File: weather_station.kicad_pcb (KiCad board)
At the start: 2 copper layers, 91.4 x 43.2 mm, 20 parts, among them J1 Barrel_Jack, U1 L7805, U2 LD1117S33TR, U6 NRF24L01_Breakout, U7 ATmega328-PU, Y1 16Mhz

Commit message: Poprawiona płytka (konektor NRF24 oraz otwory na śrubki)
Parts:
- U6: footprint RF_Module:nRF24L01_Breakout -> weather_station:NRF24-horizontal-pin-socket
- moved U6 11.4 mm to (146.6, 123.1), turned to 180 degrees
- moved C5 2.80 mm to (149.2, 107.7)
- renumbered RTC to U3, DHT22 to U4, LCD to U5
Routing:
- net /CSN: track 17.7 -> 6.76 mm
- net /MOSI: track 15.3 -> 5.70 mm
- net /SCK: track 10.3 -> 15.2 mm
- net /CE: track 13.4 -> 9.30 mm
- net +3V3: track 94.1 -> 97.3 mm
- net /MISO: track 10.3 -> 9.40 mm
- net GND: vias 28 -> 40

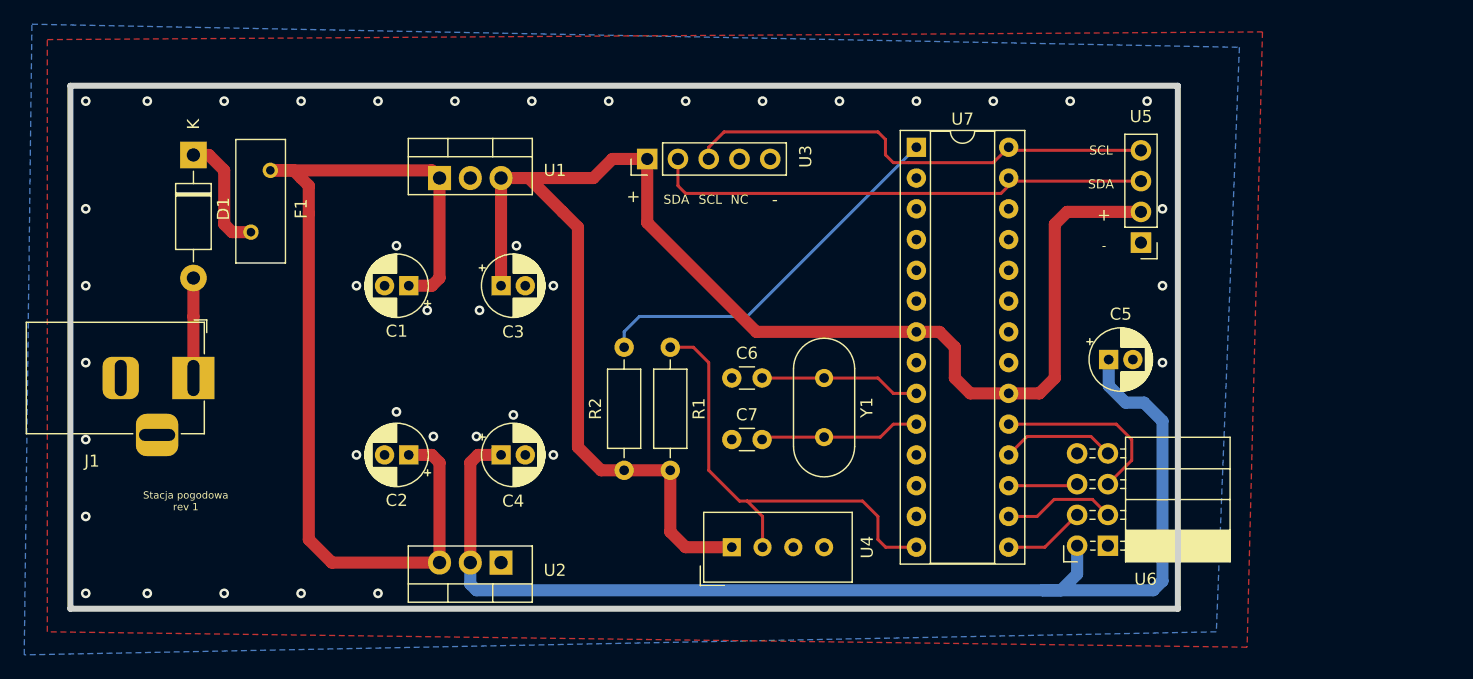
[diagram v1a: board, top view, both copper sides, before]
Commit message: Zmiana otworów na śruby z M2 na M3
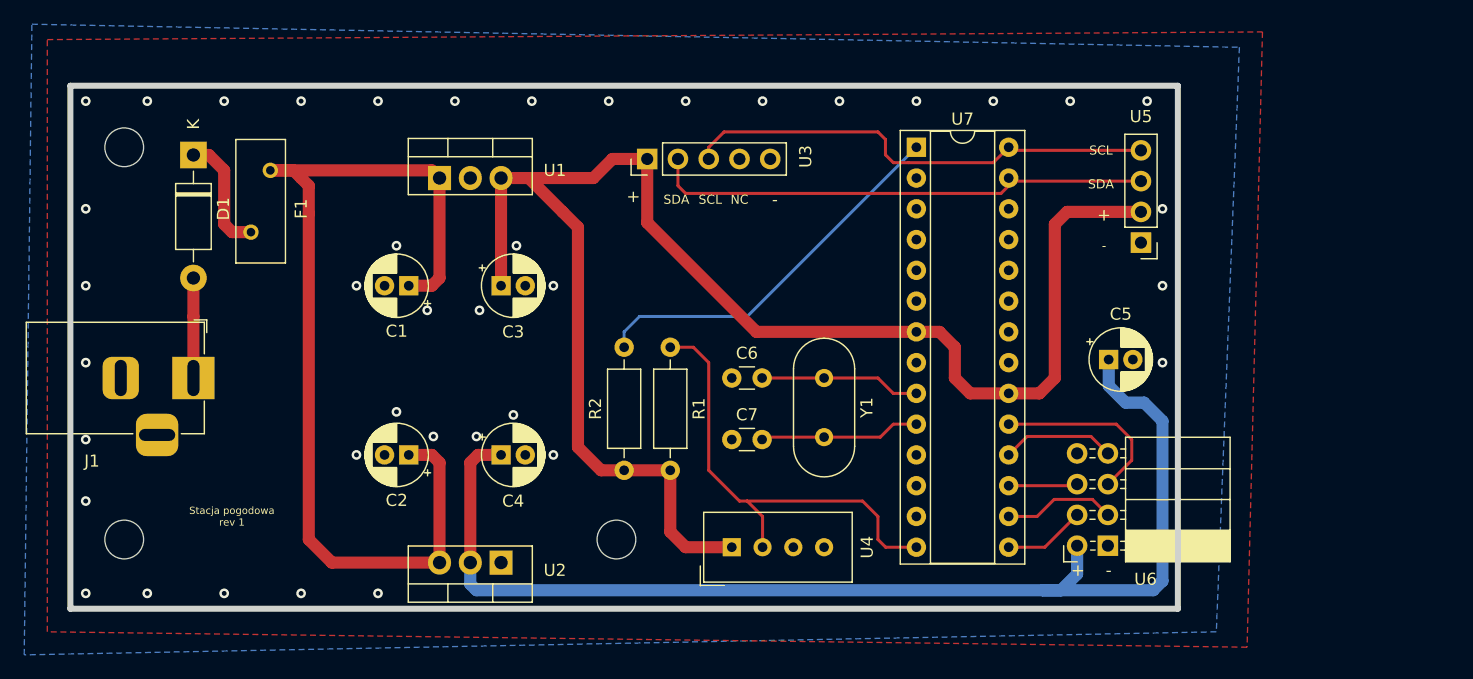
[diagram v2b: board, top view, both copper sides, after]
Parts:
- added REF**: MountingHole_3.2mm_M3, MountingHole:MountingHole_3.2mm_M3, F.Cu at (108.6, 122.6)
- added REF**: MountingHole_3.2mm_M3, MountingHole:MountingHole_3.2mm_M3, F.Cu at (67.9, 90.2)
- added REF**: MountingHole_3.2mm_M3, MountingHole:MountingHole_3.2mm_M3, F.Cu at (67.9, 122.6)
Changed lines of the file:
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@@
   (general
     (thickness 1.6)
-    (drawings 16)
+    (drawings 18)
     (tracks 165)
     (zones 0)
-    (modules 20)
+    (modules 23)
     (nets 34)
   )
@@
     (mod_text_size 1 1)
     (mod_text_width 0.15)
-    (pad_size 1.524 1.524)
-    (pad_drill 0.762)
+    (pad_size 2.2 2.2)
+    (pad_drill 2.2)
     (pad_to_mask_clearance 0)
     (aux_axis_origin 0 0)
@@
     (add_net "Net-(U7-Pad5)")
     (add_net "Net-(U7-Pad6)")
+  )
+  (module MountingHole:MountingHole_3.2mm_M3 (layer F.Cu)
+    (at 108.585 122.555)
+    (descr "Mounting Hole 3.2mm, no annular, M3")
+    (tags "mounting hole 3.2mm no annular m3")
+    (attr virtual)
+    (fp_text reference REF** (at 0 -4.2) (layer F.SilkS) hide
+      (effects (font (size 1 1) (thickness 0.15)))
+    )
+    (fp_text value MountingHole_3.2mm_M3 (at 0 4.2) (layer F.Fab)
+      (effects (font (size 1 1) (thickness 0.15)))
+    )
+    (fp_text user %R (at 0.3 0) (layer F.Fab)
+      (effects (font (size 1 1) (thickness 0.15)))
+    )
+    (fp_circle (center 0 0) (end 3.2 0) (layer Cmts.User) (width 0.15))
+    (fp_circle (center 0 0) (end 3.45 0) (layer F.CrtYd) (width 0.05))
+    (pad 1 np_thru_hole circle (at 0 0) (size 3.2 3.2) (drill 3.2) (layers *.Cu *.Mask))
+  )
+  (module MountingHole:MountingHole_3.2mm_M3 (layer F.Cu)
+    (at 67.945 90.17)
+    (descr "Mounting Hole 3.2mm, no annular, M3")
+    (tags "mounting hole 3.2mm no annular m3")
+    (attr virtual)
+    (fp_text reference REF** (at 0 -4.2) (layer F.SilkS) hide
+      (effects (font (size 1 1) (thickness 0.15)))
+    )
+    (fp_text value MountingHole_3.2mm_M3 (at 0 4.2) (layer F.Fab)
+      (effects (font (size 1 1) (thickness 0.15)))
+    )
+    (fp_text user %R (at 0.3 0) (layer F.Fab)
+      (effects (font (size 1 1) (thickness 0.15)))
+    )
+    (fp_circle (center 0 0) (end 3.2 0) (layer Cmts.User) (width 0.15))
+    (fp_circle (center 0 0) (end 3.45 0) (layer F.CrtYd) (width 0.05))
+    (pad 1 np_thru_hole circle (at 0 0) (size 3.2 3.2) (drill 3.2) (layers *.Cu *.Mask))
+  )
+  (module MountingHole:MountingHole_3.2mm_M3 (layer F.Cu)
+    (at 67.945 122.555)
+    (descr "Mounting Hole 3.2mm, no annular, M3")
+    (tags "mounting hole 3.2mm no annular m3")
+    (attr virtual)
+    (fp_text reference REF** (at 0 -4.2) (layer F.SilkS) hide
+      (effects (font (size 1 1) (thickness 0.15)))
+    )
+    (fp_text value MountingHole_3.2mm_M3 (at 0 4.2) (layer F.Fab)
+      (effects (font (size 1 1) (thickness 0.15)))
+    )
+    (fp_text user %R (at 0.3 0) (layer F.Fab)
+      (effects (font (size 1 1) (thickness 0.15)))
+    )
+    (fp_circle (center 0 0) (end 3.2 0) (layer Cmts.User) (width 0.15))
+    (fp_circle (center 0 0) (end 3.45 0) (layer F.CrtYd) (width 0.05))
+    (pad 1 np_thru_hole circle (at 0 0) (size 3.2 3.2) (drill 3.2) (layers *.Cu *.Mask))
   )
   (module Connector_PinHeader_2.54mm:PinHeader_1x04_P2.54mm_Vertical (layer F.Cu)
@@
     )
   )
-  (gr_text "Stacja pogodowa \nrev 1" (at 73.025 119.38) (layer F.SilkS)
+  (gr_text - (at 149.225 125.095) (layer F.SilkS)
+    (effects (font (size 1 1) (thickness 0.15)))
+  )
+  (gr_text + (at 146.685 125.095) (layer F.SilkS)
+    (effects (font (size 1 1) (thickness 0.15)))
+  )
+  (gr_text "Stacja pogodowa \nrev 1" (at 76.835 120.65) (layer F.SilkS)
     (effects (font (size 0.6 0.6) (thickness 0.15)))
   )
@@
   (via (at 64.77 107.95) (size 0.8) (drill 0.4) (layers F.Cu B.Cu) (net 2))
   (via (at 64.77 114.3) (size 0.8) (drill 0.4) (layers F.Cu B.Cu) (net 2))
-  (via (at 64.77 120.65) (size 0.8) (drill 0.4) (layers F.Cu B.Cu) (net 2))
+  (via (at 64.77 119.38) (size 0.8) (drill 0.4) (layers F.Cu B.Cu) (net 2))
   (via (at 64.77 127) (size 0.8) (drill 0.4) (layers F.Cu B.Cu) (net 2))
   (via (at 69.85 127) (size 0.8) (drill 0.4) (layers F.Cu B.Cu) (net 2))

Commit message: Wersja wysłana do produkcji
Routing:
- net +3V3: track 97.3 -> 93.1 mm
- net GND: vias 40 -> 44
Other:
- rule trace_min: 0.1016 -> 0.15
- rule via_min_drill: 0.3 -> 0.35
- rule via_min_size: 0.4 -> 0.6
